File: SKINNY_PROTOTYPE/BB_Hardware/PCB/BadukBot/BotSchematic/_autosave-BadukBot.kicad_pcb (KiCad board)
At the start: 4 copper layers, 22.4 x 87.6 mm, 72 parts, among them J1 MOLEX_78171-0002, J10 A3-16DA-2SV(71), J11 62401621722, J12 803-87-010-10-001101, J13 67997-410HLF, J2 MOLEX_78171-0003, Q1 MMBT3904LT1G, Q2 MMBT3904LT1G, Q3 MMBT3904LT1G, Q4 MMBT3904LT1G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

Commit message: More work on the PCB
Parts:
- moved U2 3.24 mm to (225.3, 97.2), turned to 45 degrees
- moved U3 3.05 mm to (216.2, 146.2)
- moved U5 2.67 mm to (220.3, 73.4), turned to 45 degrees
- moved C9 2.08 mm to (214.8, 152.1), turned to 90 degrees
- moved C1 1.20 mm to (218.2, 154.2)
- moved C2 1.20 mm to (218.3, 155.7)
- moved C4 1.20 mm to (219.0, 152.2)
- moved C5 1.20 mm to (217.5, 152.2)
- moved C3 1.10 mm to (220.7, 153.2)
- moved C22 1.01 mm to (218.3, 143.4)
- moved R4 0.98 mm to (222.7, 141.1)
- moved R27 0.67 mm to (215.9, 142.9), turned to 180 degrees
- moved U1 0.66 mm to (224.6, 146.8), turned to 45 degrees
- turned U7 to 145 degrees

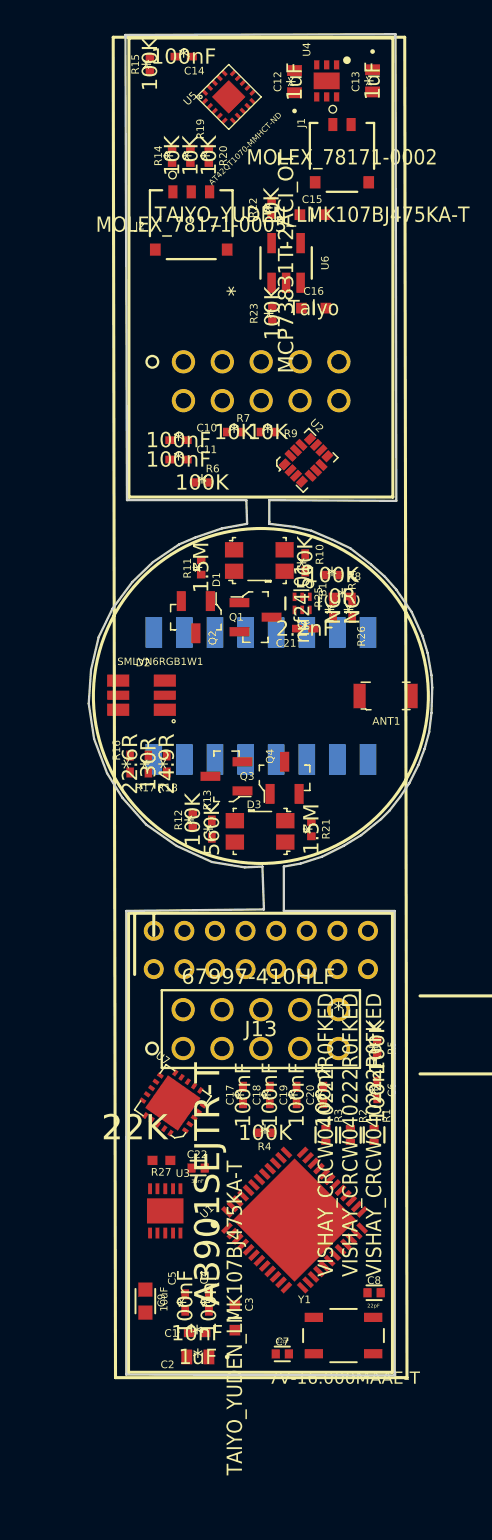
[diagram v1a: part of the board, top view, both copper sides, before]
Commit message: Original board layer images added; Experiments with trace routing using FreeRouting and component placement in KiCAD
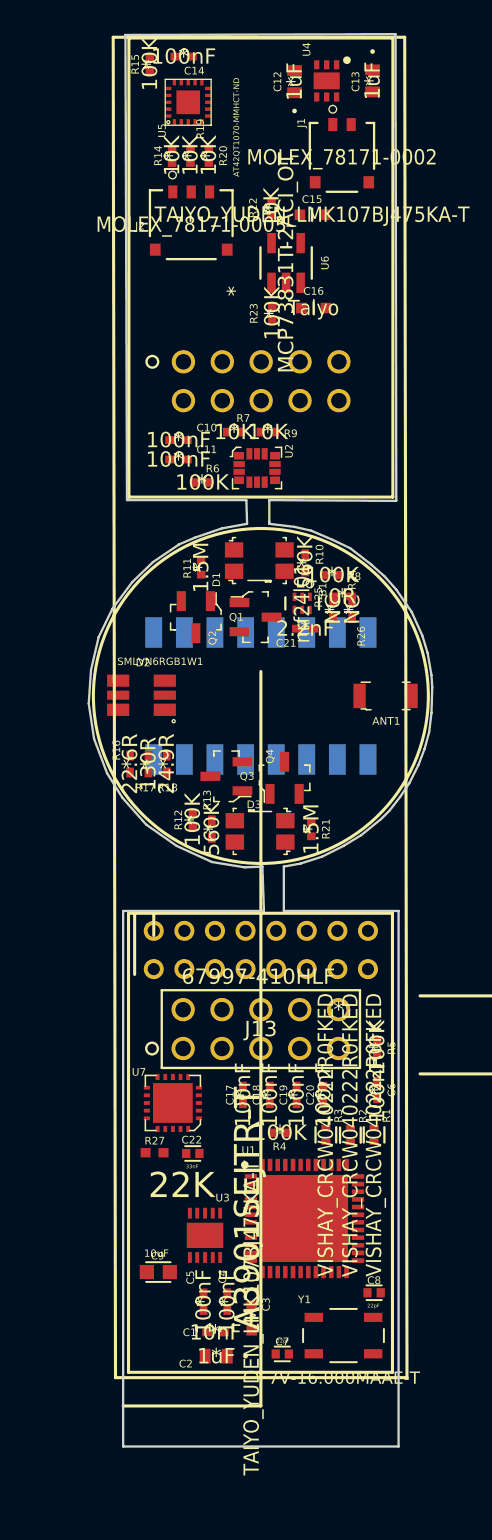
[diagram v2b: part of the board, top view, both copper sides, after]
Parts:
- moved U2 3.24 mm to (222.2, 97.7), turned to 0 degrees
- moved U3 3.05 mm to (218.8, 147.8)
- moved U5 2.67 mm to (217.7, 73.8), turned to 90 degrees
- moved C9 2.08 mm to (215.7, 150.2), turned to 180 degrees
- moved C1 1.20 mm to (219.4, 154.1)
- moved C2 1.20 mm to (219.5, 155.7)
- moved C4 1.20 mm to (220.2, 152.1)
- moved C5 1.20 mm to (218.7, 152.1)
- moved C3 1.10 mm to (221.8, 153.2)
- moved C22 1.01 mm to (217.9, 142.4)
- moved R4 0.98 mm to (223.7, 141.1)
- moved R27 0.67 mm to (215.4, 142.4), turned to 0 degrees
- moved U1 0.66 mm to (225.2, 146.7), turned to 0 degrees
- turned U7 to 180 degrees
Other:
- board size 22.4 x 87.6 mm -> 22.4 x 92.3 mm
- net class Default: clearance 0.2 -> 0.127; trace_width 0.25 -> 0.1524; via_dia 0.8 -> 0.254; via_drill 0.4 -> 0.1016
- rule pad_to_mask_clearance: 0.2 -> 0.0508
- rule trace_clearance: 0.2 -> 0.127
- rule trace_min: 0.2 -> 0.127
- rule via_min_drill: 0.3 -> 0.0508
- rule via_min_size: 0.4 -> 0.254

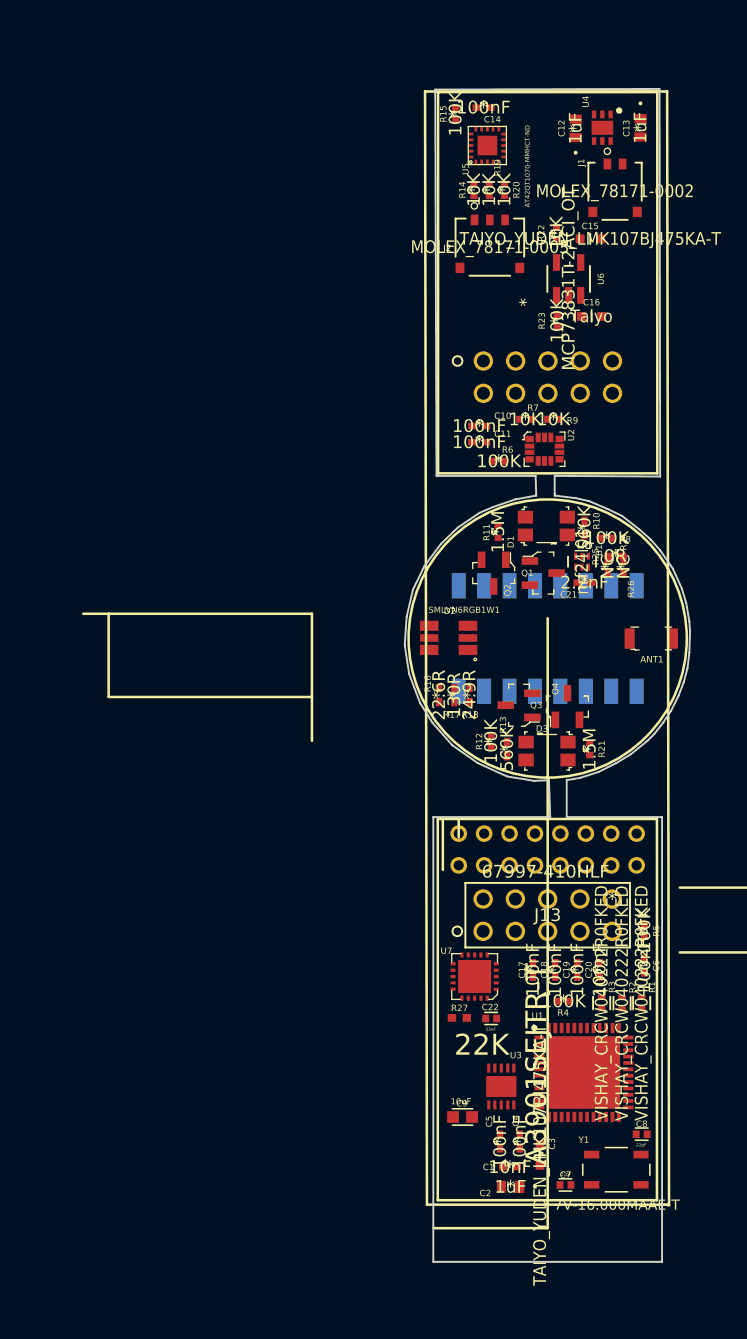
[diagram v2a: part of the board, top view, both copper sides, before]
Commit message: Board adjustments for main board and topboard connectors
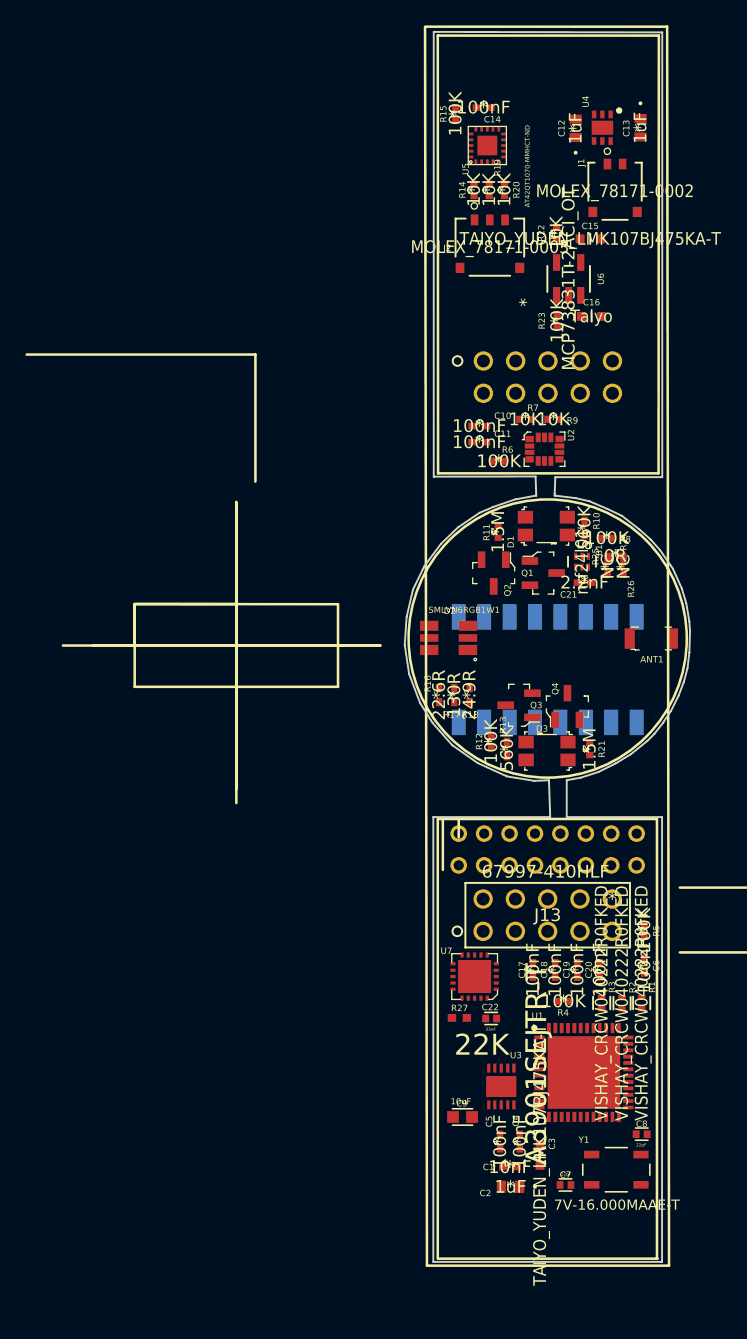
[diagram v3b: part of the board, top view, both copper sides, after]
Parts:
- moved J10 2.45 mm to (222.4, 115.0)
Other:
- board size 22.4 x 92.3 mm -> 22.4 x 96.8 mm
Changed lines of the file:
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@@
   (general
     (thickness 1.6)
-    (drawings 81)
+    (drawings 108)
     (tracks 0)
     (zones 0)
@@
     (39 F.Mask user)
     (40 Dwgs.User user)
-    (41 Cmts.User user)
+    (41 Cmts.User user hide)
     (42 Eco1.User user)
     (43 Eco2.User user)
@@
     (pad_to_mask_clearance 0.0508)
     (aux_axis_origin 0 0)
-    (visible_elements FFFDFF7F)
+    (visible_elements FFFDF7FF)
     (pcbplotparams
       (layerselection 0x010fc_ffffffff)
@@
   )
   (module 16pos_2mm_SMD:A13 (layer B.Cu)
-    (at 222.4 112.55 180)
+    (at 222.4 115 180)
     (descr "16 Position Receptacle Connector 0.079\" (2.00mm) Surface Mount Gold")
     (attr smd)
@@
       (net 123 1b_3.3v))
   )
-  (gr_line (start 222.4 158.95) (end 222.4 110.95) (layer F.SilkS) (width 0.2))
-  (gr_line (start 213.4 158.95) (end 222.4 158.95) (layer F.SilkS) (width 0.2))
-  (gr_line (start 213.65 99.75) (end 213.55 69.35) (layer Edge.Cuts) (width 0.15))
-  (gr_line (start 221.45 99.75) (end 213.65 99.75) (layer Edge.Cuts) (width 0.15))
-  (gr_line (start 221.5 101.3) (end 221.45 99.75) (layer Edge.Cuts) (width 0.15))
+  (gr_line (start 206.9 117.95) (end 206.9 116.65) (layer B.SilkS) (width 0.2))
+  (gr_line (start 188.9 108.2) (end 188.9 106.55) (layer B.SilkS) (width 0.2))
+  (gr_line (start 188.9 106.55) (end 197.9 106.55) (layer B.SilkS) (width 0.2))
+  (gr_line (start 206.9 108.2) (end 188.9 108.2) (layer B.SilkS) (width 0.2))
+  (gr_line (start 206.9 106.55) (end 206.9 108.2) (layer B.SilkS) (width 0.2))
+  (gr_line (start 188.9 106.55) (end 206.9 106.55) (layer B.SilkS) (width 0.2))
+  (gr_line (start 188.9 117.95) (end 197.9 117.95) (layer B.SilkS) (width 0.2))
+  (gr_line (start 188.9 119.6) (end 188.9 117.95) (layer B.SilkS) (width 0.2))
+  (gr_line (start 206.9 119.6) (end 188.9 119.6) (layer B.SilkS) (width 0.2))
+  (gr_line (start 206.9 117.95) (end 206.9 119.6) (layer B.SilkS) (width 0.2))
+  (gr_line (start 188.9 117.95) (end 206.9 117.95) (layer B.SilkS) (width 0.2))
+  (gr_line (start 197.9 101.8) (end 197.9 125.5) (layer F.SilkS) (width 0.2))
+  (gr_line (start 191.5 113.05) (end 191.5 113.1) (layer B.SilkS) (width 0.2))
+  (gr_line (start 191.5 108.3) (end 191.5 113.05) (layer B.SilkS) (width 0.2))
+  (gr_line (start 197.85 108.3) (end 197.9 108.3) (layer B.SilkS) (width 0.2))
+  (gr_line (start 197.9 108.3) (end 204.25 108.3) (layer B.SilkS) (width 0.2))
+  (gr_line (start 191.5 108.3) (end 204.25 108.3) (layer B.SilkS) (width 0.2))
+  (gr_line (start 191.5 117.85) (end 191.5 108.3) (layer B.SilkS) (width 0.2))
+  (gr_line (start 204.25 117.85) (end 191.5 117.85) (layer B.SilkS) (width 0.2))
+  (gr_line (start 204.25 108.3) (end 204.25 117.85) (layer B.SilkS) (width 0.2))
+  (gr_line (start 209.15 113.1) (end 197.9 113.1) (layer F.SilkS) (width 0.2))
+  (gr_line (start 197.9 124.35) (end 197.9 113.1) (layer F.SilkS) (width 0.2))
+  (gr_line (start 197.9 124.35) (end 197.9 101.85) (layer F.SilkS) (width 0.2))
+  (gr_line (start 186.65 113.1) (end 209.15 113.1) (layer F.SilkS) (width 0.2))
+  (gr_line (start 189.90348 109.834682) (end 197.90348 109.834682) (layer F.SilkS) (width 0.2))
+  (gr_line (start 189.9 113.1) (end 189.9 109.85) (layer F.SilkS) (width 0.2))
+  (gr_line (start 205.9 109.85) (end 205.9 116.35) (layer F.SilkS) (width 0.2))
+  (gr_line (start 205.9 109.85) (end 189.90348 109.834682) (layer F.SilkS) (width 0.2))
+  (gr_line (start 184.25 113.1) (end 209.25 113.1) (layer F.SilkS) (width 0.2))
+  (gr_line (start 213.43389 99.810135) (end 213.43389 64.810135) (layer Edge.Cuts) (width 0.15))
+  (gr_line (start 213.43389 64.810135) (end 231.416945 64.85) (layer Edge.Cuts) (width 0.15))
+  (gr_line (start 231.416945 64.85) (end 231.416945 99.85) (layer Edge.Cuts) (width 0.15))
+  (gr_line (start 221.45 99.8) (end 213.43389 99.810135) (layer Edge.Cuts) (width 0.15))
+  (gr_line (start 221.5 101.3) (end 221.45 99.8) (layer Edge.Cuts) (width 0.15))
   (gr_line (start 219.85 101.6) (end 221.5 101.3) (layer Edge.Cuts) (width 0.15))
   (gr_line (start 218.1 102.2) (end 219.85 101.6) (layer Edge.Cuts) (width 0.15))
@@
   (gr_line (start 222.95 101.3) (end 224.6 101.5) (layer Edge.Cuts) (width 0.15))
   (gr_line (start 222.95 101.15) (end 222.95 101.3) (layer Edge.Cuts) (width 0.15))
-  (gr_line (start 222.95 99.75) (end 222.95 101.15) (layer Edge.Cuts) (width 0.15))
-  (gr_line (start 231.25 99.8) (end 222.95 99.75) (layer Edge.Cuts) (width 0.15))
-  (gr_line (start 231.2 69.3) (end 231.25 99.8) (layer Edge.Cuts) (width 0.15))
-  (gr_line (start 213.55 69.35) (end 231.2 69.3) (layer Edge.Cuts) (width 0.15))
-  (gr_line (start 213.75 126.8) (end 213.75 156.75) (layer F.SilkS) (width 0.2))
-  (gr_line (start 231 156.75) (end 213.75 156.75) (layer F.SilkS) (width 0.2))
-  (gr_line (start 231 126.75) (end 231 156.75) (layer F.SilkS) (width 0.2))
+  (gr_line (start 223 99.85) (end 222.95 101.15) (layer Edge.Cuts) (width 0.15))
+  (gr_line (start 231.416945 99.85) (end 223 99.85) (layer Edge.Cuts) (width 0.15))
+  (gr_line (start 213.75 126.8) (end 213.75 161.35) (layer F.SilkS) (width 0.2))
+  (gr_line (start 231.05 161.35) (end 213.8 161.35) (layer F.SilkS) (width 0.2))
+  (gr_line (start 231 126.75) (end 231 161.35) (layer F.SilkS) (width 0.2))
   (gr_line (start 213.75 126.75) (end 231 126.75) (layer F.SilkS) (width 0.2))
-  (gr_line (start 213.775 99.55) (end 213.775 69.55) (layer F.SilkS) (width 0.2))
-  (gr_line (start 231.025 99.55) (end 213.775 99.55) (layer F.SilkS) (width 0.2))
-  (gr_line (start 231.025 69.55) (end 231.025 99.55) (layer F.SilkS) (width 0.2))
-  (gr_line (start 213.775 69.55) (end 231.025 69.55) (layer F.SilkS) (width 0.2))
+  (gr_line (start 213.775 99.55) (end 213.75 65.1) (layer F.SilkS) (width 0.2))
+  (gr_line (start 231.1 99.55) (end 213.775 99.55) (layer F.SilkS) (width 0.2))
+  (gr_line (start 231.15 65.1) (end 231.125 99.55) (layer F.SilkS) (width 0.2))
+  (gr_line (start 213.75 65.1) (end 231.15 65.1) (layer F.SilkS) (width 0.2))
   (gr_line (start 245.5 137.25) (end 245.5 132.15) (layer F.SilkS) (width 0.2))
   (gr_line (start 245.5 132.15) (end 232.8 132.15) (layer F.SilkS) (width 0.2))
@@
   (gr_line (start 214.15 130.75) (end 214.15 126.75) (layer F.SilkS) (width 0.2))
   (gr_circle (center 222.4 112.55) (end 214.2 119.8) (layer F.SilkS) (width 0.2))
-  (gr_line (start 203.85 110.6) (end 185.85 110.6) (layer F.SilkS) (width 0.2))
-  (gr_line (start 187.85 117.15) (end 203.85 117.15) (layer F.SilkS) (width 0.2))
-  (gr_line (start 187.85 117.1) (end 187.85 110.6) (layer F.SilkS) (width 0.2))
-  (gr_line (start 203.85 110.6) (end 203.85 120.6) (layer F.SilkS) (width 0.2))
-  (gr_line (start 212.9 157.1) (end 212.75 69.5) (layer F.SilkS) (width 0.2))
-  (gr_line (start 231.95 157.1) (end 212.9 157.1) (layer F.SilkS) (width 0.2))
-  (gr_line (start 231.8 69.5) (end 231.95 157.1) (layer F.SilkS) (width 0.2))
-  (gr_line (start 212.75 69.5) (end 231.8 69.5) (layer F.SilkS) (width 0.2))
+  (gr_line (start 199.4 90.2) (end 181.4 90.2) (layer F.SilkS) (width 0.2))
+  (gr_line (start 189.9 116.35) (end 205.9 116.35) (layer F.SilkS) (width 0.2))
+  (gr_line (start 189.9 116.35) (end 189.9 109.85) (layer F.SilkS) (width 0.2))
+  (gr_line (start 199.4 90.2) (end 199.4 100.2) (layer F.SilkS) (width 0.2))
+  (gr_line (start 212.9 161.9) (end 212.75 64.45) (layer F.SilkS) (width 0.2))
+  (gr_line (start 231.95 161.9) (end 212.9 161.9) (layer F.SilkS) (width 0.2))
+  (gr_line (start 231.8 64.4) (end 231.95 161.9) (layer F.SilkS) (width 0.2))
+  (gr_line (start 212.75 64.4) (end 231.8 64.4) (layer F.SilkS) (width 0.2))
 )

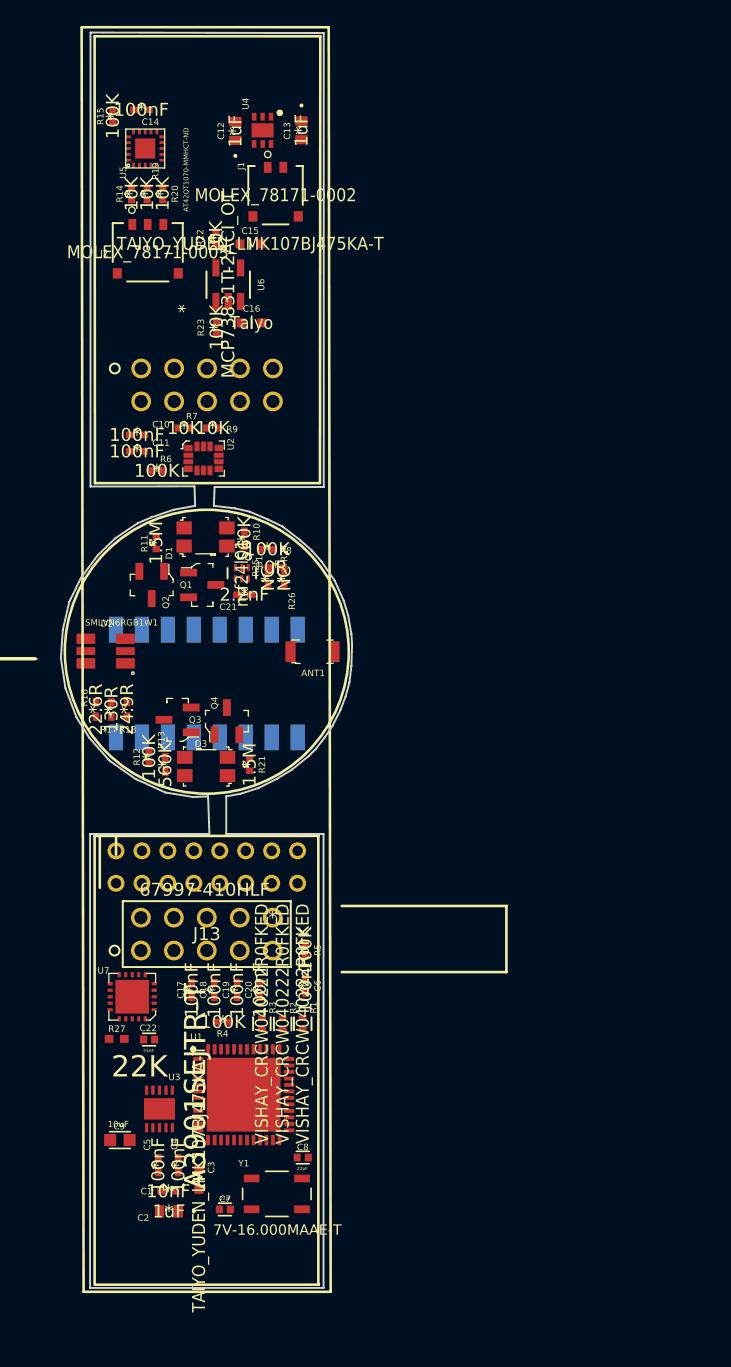
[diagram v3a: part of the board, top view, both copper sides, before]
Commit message: Added graphics and logos for silk screen
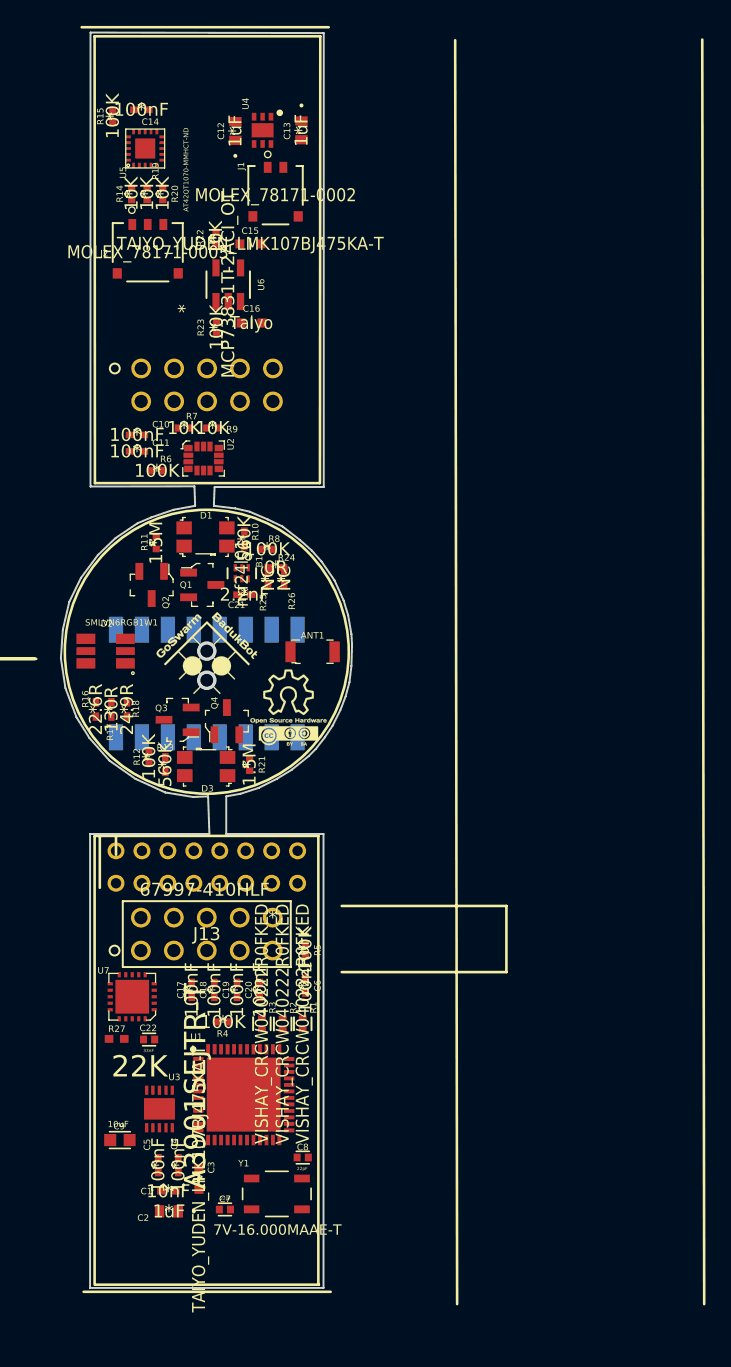
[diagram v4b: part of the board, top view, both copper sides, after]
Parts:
- added G***: LOGO, Silk:OpenHardwareLogo, F.Cu at (228.7, 116.8)
- added G***: LOGO, Silk:BadukBot-GoSwarm, F.Cu at (222.4, 112.8)
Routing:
- net (no net): vias 0 -> 2
